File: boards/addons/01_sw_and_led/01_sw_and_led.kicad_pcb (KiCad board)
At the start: 2 copper layers, 47.5 x 72 mm, 8 parts, among them SW1 SW_Push, SW2 SW_Push

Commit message: ピンソケット配置
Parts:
- added J1: Conn_01x04_Socket, Connector_PinSocket_2.54mm:PinSocket_1x04_P2.54mm_Vertical, F.Cu at (137.2, 71.1)
- added J2: Conn_01x04_Socket, Connector_PinSocket_2.54mm:PinSocket_1x04_P2.54mm_Vertical, F.Cu at (132.1, 101.6)

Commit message: 配置調整
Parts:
- moved R1 10.5 mm to (139.7, 101.6), turned to 0 degrees
- moved R2 10.5 mm to (139.7, 121.9), turned to 0 degrees
- moved SW1 7.62 mm to (156.3, 101.6)
- moved SW2 7.62 mm to (156.3, 122.0)

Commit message: AW 引いた
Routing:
- net /SW2: track 0.00 -> 71.3 mm
- net /SW1: track 0.00 -> 42.2 mm
- net +3.3V: track 0.00 -> 30.0 mm
- net /LED2: track 0.00 -> 17.3 mm
- net /LED1: track 0.00 -> 13.0 mm
- net Net-(D2-A): track 0.00 -> 5.08 mm
- net Net-(D1-A): track 0.00 -> 5.08 mm
- added copper zone on B.Cu, net GND
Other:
- board text added: "LED1"
- board text added: "LED2"
- board text added: "SW and LED board for digital IO v0.1"
- board text added: "SW1"
- board text added: "SW2"

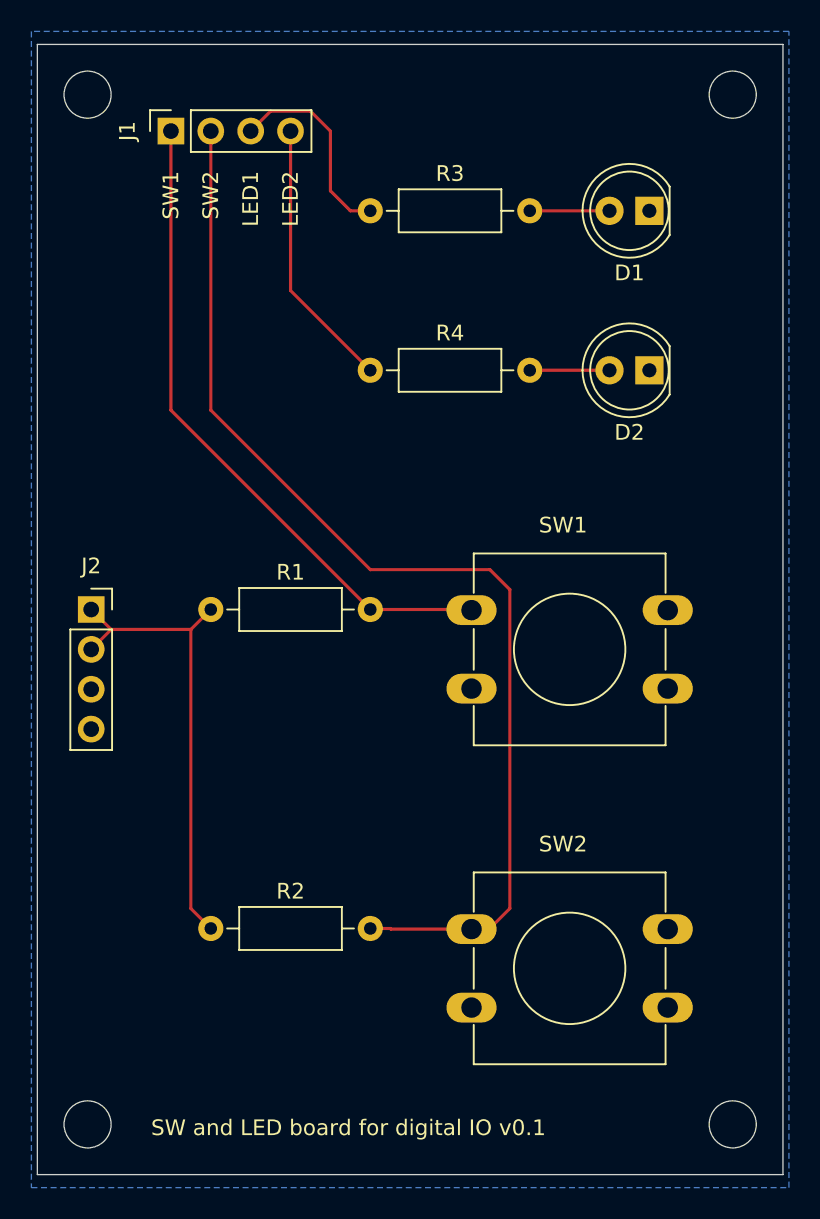
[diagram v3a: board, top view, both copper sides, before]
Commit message: スイッチのプルアップ抵抗はなくしました
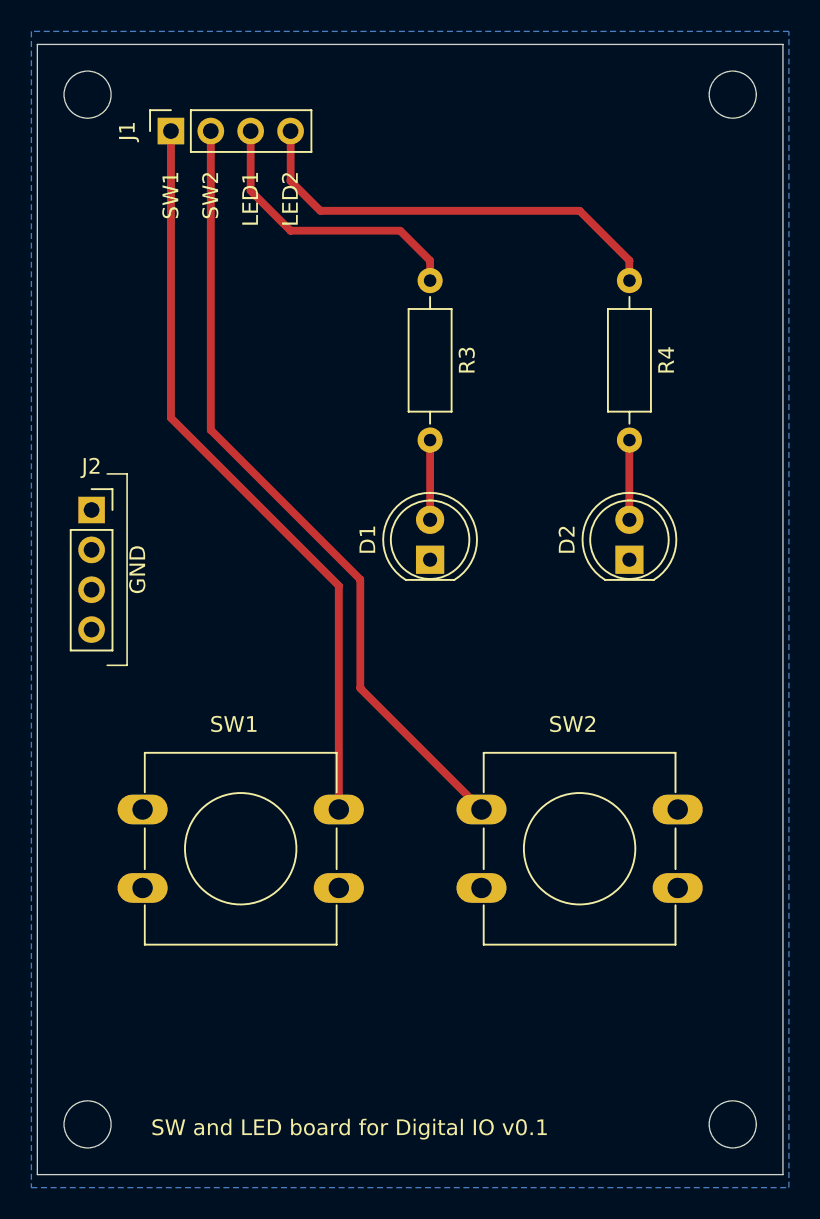
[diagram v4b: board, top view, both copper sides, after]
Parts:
- removed R1, R2: R, Resistor_THT:R_Axial_DIN0207_L6.3mm_D2.5mm_P10.16mm_Horizontal
- moved D1 26.3 mm to (153.7, 98.4), turned to 90 degrees
- moved SW1 24.5 mm to (135.4, 114.3)
- moved R4 17.5 mm to (166.4, 80.6), turned to -90 degrees
- moved D2 12.1 mm to (166.4, 98.4), turned to 90 degrees
- moved SW2 7.65 mm to (156.9, 114.3)
- moved J2 6.34 mm to (132.1, 95.3)
- moved R3 5.85 mm to (153.7, 80.6), turned to -90 degrees
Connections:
- J2 pad 1: +3.3V -> GND
- J2 pad 2: +3.3V -> GND
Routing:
- net +3.3V: track 30.0 -> 0.00 mm
- net /SW2: track 71.3 -> 50.4 mm
- net /LED2: track 17.3 -> 28.1 mm
- net /SW1: track 42.2 -> 47.7 mm
- net /LED1: track 13.0 -> 18.4 mm
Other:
- board text added: "GND"
- board text added: "SW and LED board for Digital IO v0.1"
- board text removed: "SW and LED board for digital IO v0.1"
